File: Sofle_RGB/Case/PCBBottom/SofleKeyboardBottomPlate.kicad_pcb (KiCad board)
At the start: 2 copper layers, 143.4 x 111.8 mm, 15 parts

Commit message: things
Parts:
- removed G***: LOGO, Dane:gecko-logo
- removed G*** (x2): LOGO, Dane:big gecko
- removed G***: LOGO, dane:gecko-logo
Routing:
- added copper zone on B.Cu, net (none)
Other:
- net class Default removed
- rule pad_to_mask_clearance: 0.2 -> 0
- board text removed: "Original Sofle design by Josef Adamacik"
- board text removed: "Sofle RGB v1.0, Dane Evans"
- board text removed: "https://josefadamcik.github.io/SofleKeyboard/"

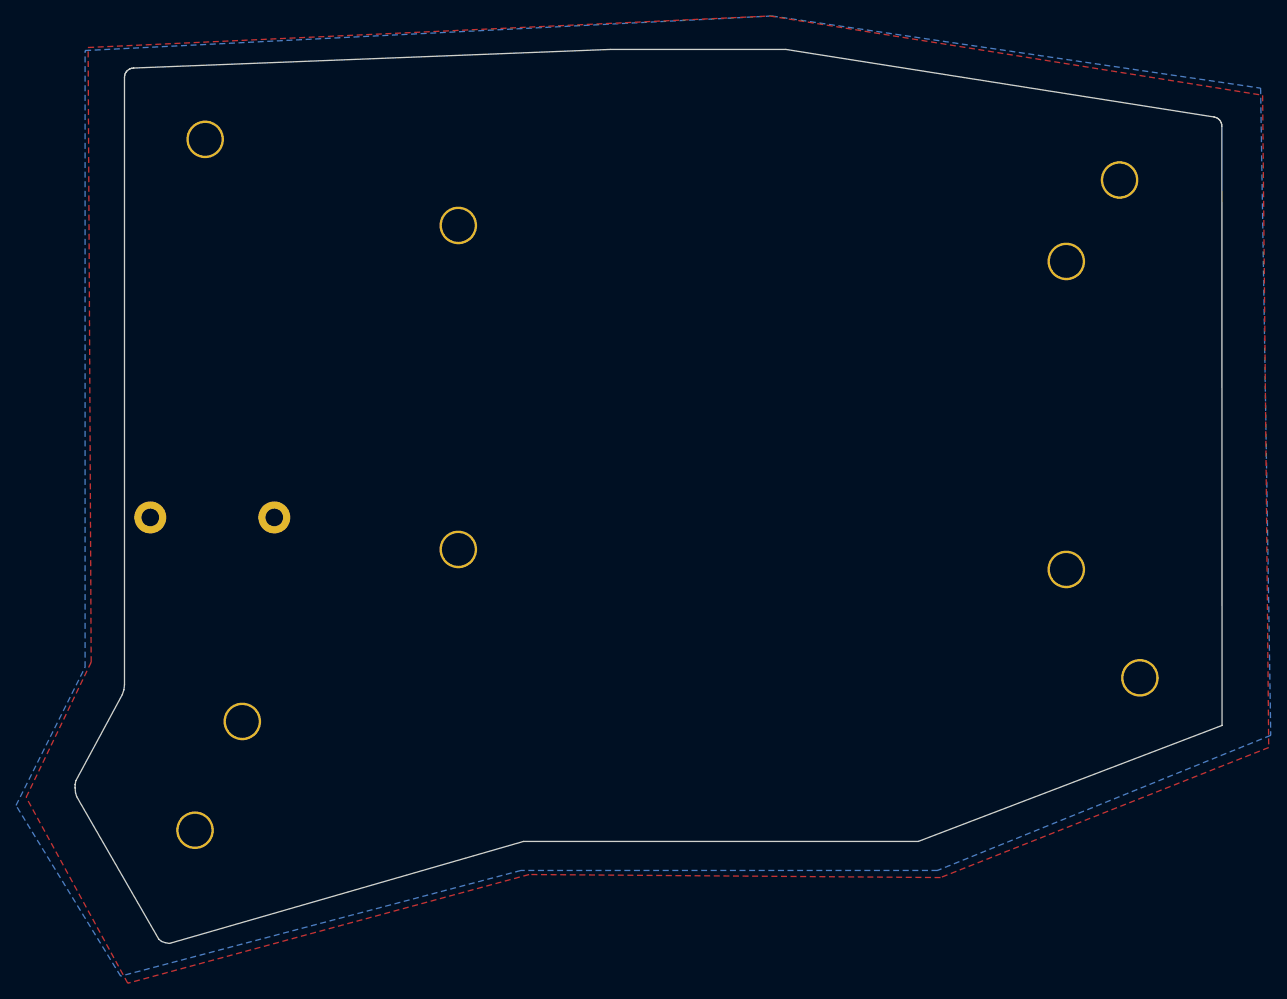
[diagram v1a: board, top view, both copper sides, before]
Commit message: fix: bottom holes
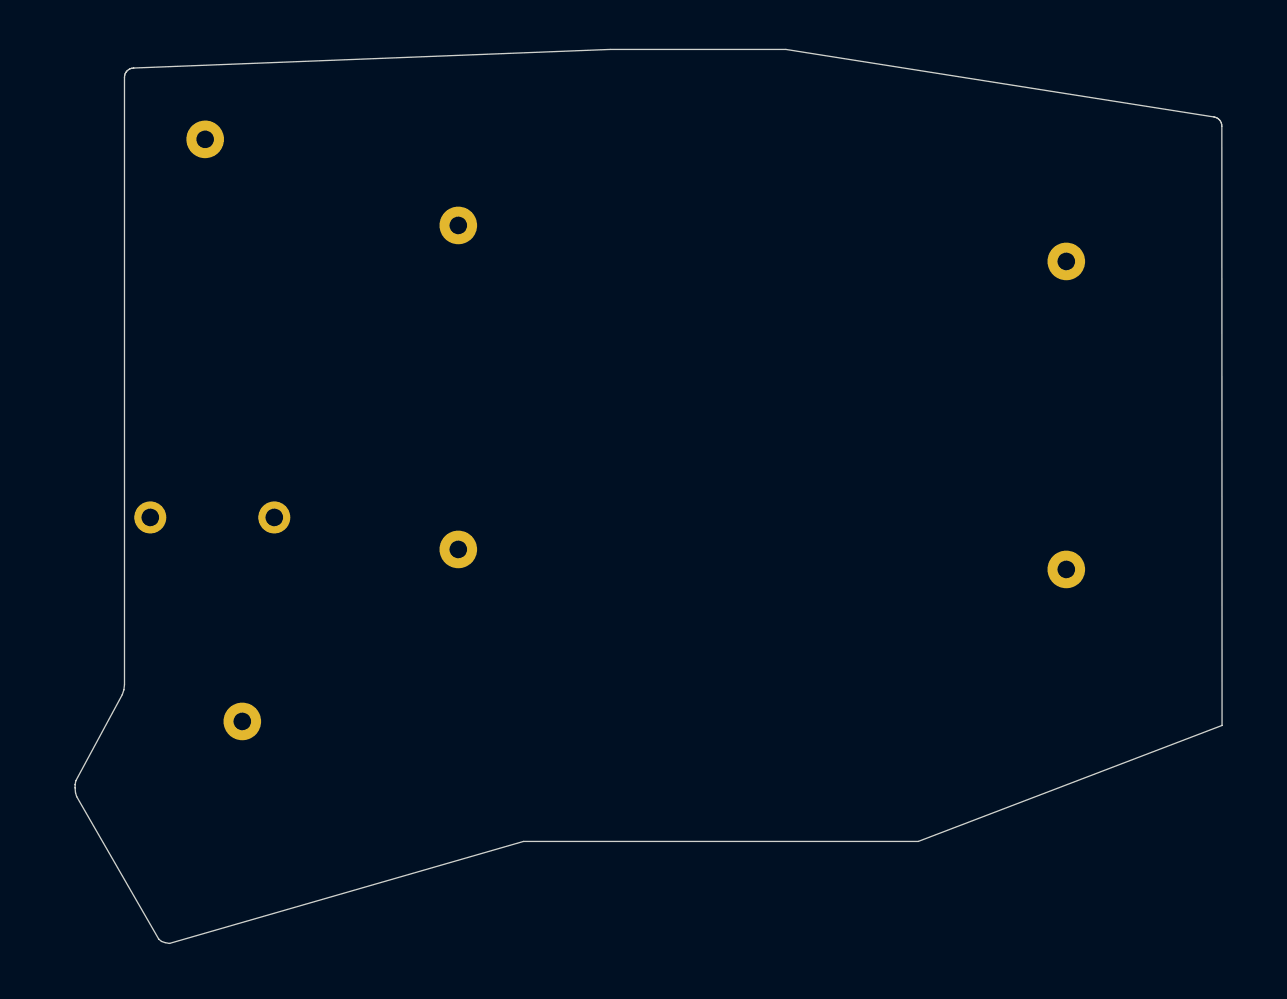
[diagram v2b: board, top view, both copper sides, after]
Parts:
- removed the TH3 at (215.9, 114.3)
- removed the TH3 at (97.8, 133.3)
- removed the TH3 at (213.4, 52.1)
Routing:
- removed copper zone on B.Cu, net (none)
- removed copper zone on F.Cu, net (none)
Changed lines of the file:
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@@
   (net 0 "")
-  (footprint "SofleKeyboard-footprint:HOLE_M2_TH" (layer "F.Cu")
-    (at 215.9 114.3)
-    (attr through_hole)
-    (fp_text reference "TH3" (at 0 -2.54) (layer "F.SilkS") hide
-      (effects (font (size 0.29972 0.29972) (thickness 0.0762)))
-    )
-    (fp_text value "HOLE" (at 0 2.54) (layer "F.SilkS") hide
-      (effects (font (size 0.29972 0.29972) (thickness 0.0762)))
-    )
-    (pad "" thru_hole circle locked (at 0.025 -0.075 90) (size 4.7 4.7) (drill 4.1) (layers *.Cu *.Mask "Dwgs.User")
-      (clearance 0.3))
-  )
   (footprint "SofleKeyboard-footprint:HOLE_M2_TH" (layer "F.Cu")
     (at 206.95 62.45)
@@
       (effects (font (size 0.29972 0.29972) (thickness 0.0762)))
     )
-    (pad "" thru_hole circle locked (at -0.225 -0.275 90) (size 4.7 4.7) (drill 4.1) (layers *.Cu *.Mask "Dwgs.User")
+    (pad "" thru_hole circle locked (at -0.225 -0.275 90) (size 4.7 4.7) (drill 2.2) (layers *.Cu *.Mask "Dwgs.User")
       (clearance 0.3))
   )
@@
       (effects (font (size 0.29972 0.29972) (thickness 0.0762)))
     )
-    (pad "" thru_hole circle locked (at 0.025 -0.075 90) (size 4.7 4.7) (drill 4.1) (layers *.Cu *.Mask "Dwgs.User")
+    (pad "" thru_hole circle locked (at 0.025 -0.075 90) (size 4.7 4.7) (drill 2.2) (layers *.Cu *.Mask "Dwgs.User")
       (clearance 0.3))
   )
@@
       (effects (font (size 0.29972 0.29972) (thickness 0.0762)))
     )
-    (pad "" thru_hole circle locked (at -0.175 -0.025 90) (size 4.7 4.7) (drill 4.1) (layers *.Cu *.Mask "Dwgs.User")
+    (pad "" thru_hole circle locked (at -0.175 -0.025 90) (size 4.7 4.7) (drill 2.2) (layers *.Cu *.Mask "Dwgs.User")
       (clearance 0.3))
   )
@@
       (effects (font (size 0.29972 0.29972) (thickness 0.0762)))
     )
-    (pad "" thru_hole circle locked (at -0.025 -0.075 90) (size 4.7 4.7) (drill 4.1) (layers *.Cu *.Mask "Dwgs.User")
+    (pad "" thru_hole circle locked (at -0.025 -0.075 90) (size 4.7 4.7) (drill 2.2) (layers *.Cu *.Mask "Dwgs.User")
       (clearance 0.3))
   )
@@
       (effects (font (size 0.29972 0.29972) (thickness 0.0762)))
     )
-    (pad "" thru_hole circle locked (at 0 0 180) (size 4.7 4.7) (drill 4.1) (layers *.Cu *.Mask "Dwgs.User")
-      (clearance 0.3))
-  )
-  (footprint "SofleKeyboard-footprint:HOLE_M2_TH" (layer "F.Cu")
-    (at 97.79 133.35)
-    (attr through_hole)
-    (fp_text reference "TH3" (at 0 -2.54) (layer "F.SilkS") hide
-      (effects (font (size 0.29972 0.29972) (thickness 0.0762)))
-    )
-    (fp_text value "HOLE" (at 0 2.54) (layer "F.SilkS") hide
-      (effects (font (size 0.29972 0.29972) (thickness 0.0762)))
-    )
-    (pad "" thru_hole circle locked (at 0.025 -0.075 90) (size 4.7 4.7) (drill 4.1) (layers *.Cu *.Mask "Dwgs.User")
-      (clearance 0.3))
-  )
-  (footprint "SofleKeyboard-footprint:HOLE_M2_TH" (layer "F.Cu")
-    (at 213.36 52.07)
-    (attr through_hole)
-    (fp_text reference "TH3" (at 0 -2.54) (layer "F.SilkS") hide
-      (effects (font (size 0.29972 0.29972) (thickness 0.0762)))
-    )
-    (fp_text value "HOLE" (at 0 2.54) (layer "F.SilkS") hide
-      (effects (font (size 0.29972 0.29972) (thickness 0.0762)))
-    )
-    (pad "" thru_hole circle locked (at 0.025 -0.075 90) (size 4.7 4.7) (drill 4.1) (layers *.Cu *.Mask "Dwgs.User")
+    (pad "" thru_hole circle locked (at 0 0 180) (size 4.7 4.7) (drill 2.2) (layers *.Cu *.Mask "Dwgs.User")
       (clearance 0.3))
   )
@@
       (effects (font (size 0.29972 0.29972) (thickness 0.0762)))
     )
-    (pad "" thru_hole circle locked (at 0.025 -0.075 90) (size 4.7 4.7) (drill 4.1) (layers *.Cu *.Mask "Dwgs.User")
+    (pad "" thru_hole circle locked (at 0.025 -0.075 90) (size 4.7 4.7) (drill 2.2) (layers *.Cu *.Mask "Dwgs.User")
       (clearance 0.3))
   )
@@
   (gr_line (start 89.000257 115.075) (end 88.998857 39.152435) (layer "Edge.Cuts") (width 0.1))
   (gr_line (start 225.586871 44.256466) (end 225.751621 44.3706) (layer "Edge.Cuts") (width 0.1))
-  (zone (net 0) (net_name "") (layer "F.Cu") (hatch edge 0.508)
-    (connect_pads (clearance 0.508))
-    (min_thickness 0.254) (filled_areas_thickness no)
-    (fill yes (thermal_gap 0.508) (thermal_bridge_width 0.508))
-    (polygon
-      (pts
-        (xy 231.267 41.402)
-        (xy 232.029 122.936)
-        (xy 191.008 139.192)
-        (xy 139.573 138.811)
-        (xy 89.408 152.4)
-        (xy 76.708 129.159)
-        (xy 84.836 112.268)
-        (xy 84.455 35.433)
-        (xy 169.672 31.496)
-      )
-    )
-  )
-  (zone (net 0) (net_name "") (layer "B.Cu") (hatch edge 0.508)
-    (connect_pads (clearance 0.508))
-    (min_thickness 0.254) (filled_areas_thickness no)
-    (fill yes (thermal_gap 0.508) (thermal_bridge_width 0.508))
-    (polygon
-      (pts
-        (xy 231.013 40.513)
-        (xy 232.283 121.412)
-        (xy 190.627 138.303)
-        (xy 138.557 138.303)
-        (xy 88.519 151.511)
-        (xy 75.438 130.175)
-        (xy 84.074 112.903)
-        (xy 84.074 35.814)
-        (xy 169.926 31.496)
-      )
-    )
-  )
 )
